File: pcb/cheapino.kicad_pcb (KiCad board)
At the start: 2 copper layers, 152.2 x 95.1 mm, 65 parts, among them K1 SW_Push, K10 SW_Push, K11 SW_Push, K12 SW_Push, K13 SW_Push, K14 SW_Push, K15 SW_Push, K16 SW_Push, K17 SW_Push, K18 SW_Push, K19 K19, K2 SW_Push, K20 K20, K21 K21, K3 SW_Push, K4 SW_Push, K5 SW_Push, K6 SW_Push, K7 SW_Push, K8 SW_Push, K9 SW_Push, U1 RP2040-Zero

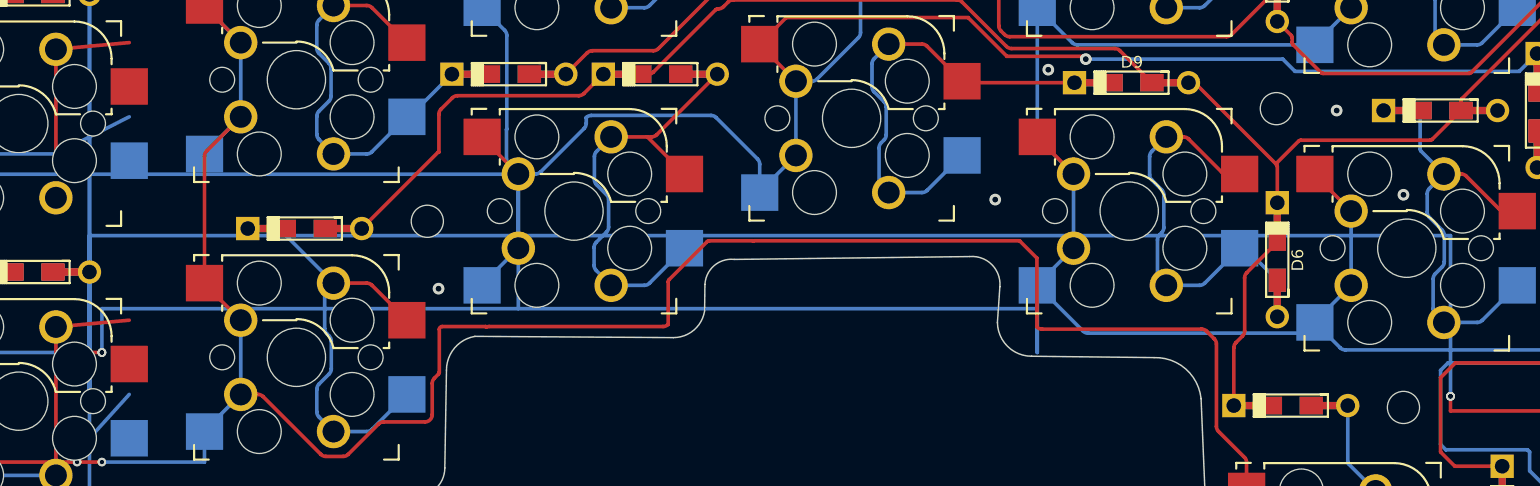
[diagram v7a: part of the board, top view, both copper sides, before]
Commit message: Re-route ROW_4 and COL_1 at y=90-92 through solid board, avoid cutout and holes
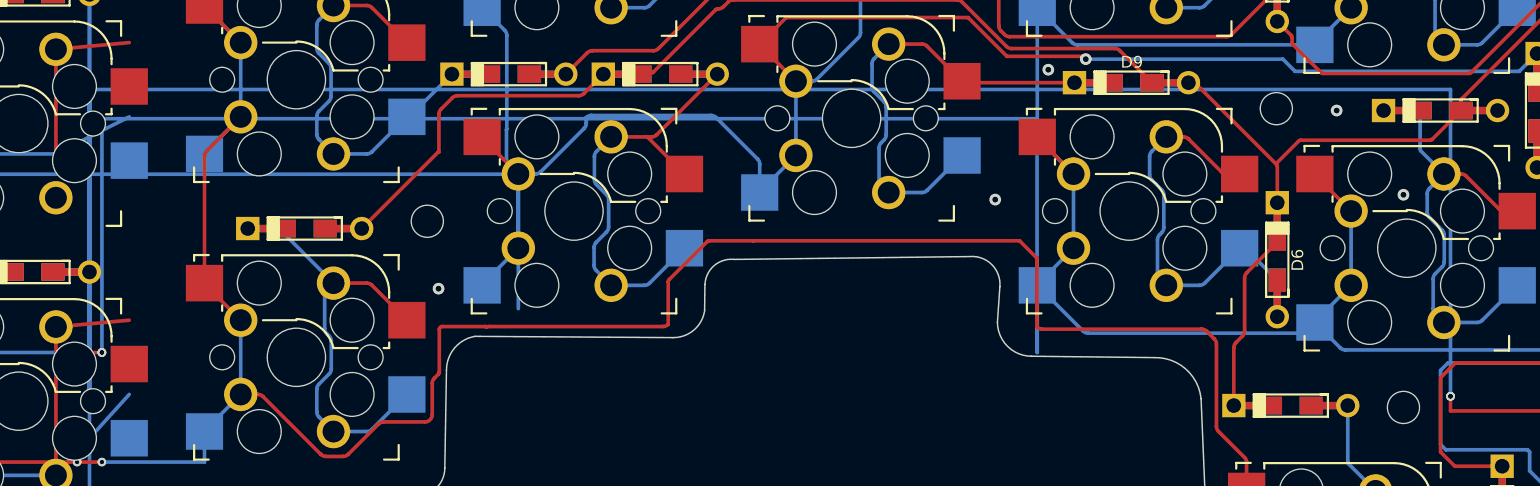
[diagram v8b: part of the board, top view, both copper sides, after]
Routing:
- net COL_1: track 385.9 -> 411.9 mm
- net ROW_4: track 270.5 -> 290.5 mm
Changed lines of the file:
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@@
 		)
 	)
+		(segment
+		(start 54.85 111.0)
+		(end 54.85 90.0)
+		(width 0.25)
+		(layer "B.Cu")
+		(net "ROW_4")
+	)
+	(segment
+		(start 54.85 90.0)
+		(end 148.0 90.0)
+		(width 0.25)
+		(layer "B.Cu")
+		(net "ROW_4")
+	)
+	(segment
+		(start 148.0 90.0)
+		(end 148.0 111.0)
+		(width 0.25)
+		(layer "B.Cu")
+		(net "ROW_4")
+	)
+	(via
+		(at 148.0 111.0)
+		(size 0.6)
+		(drill 0.3)
+		(layers "F.Cu" "B.Cu")
+		(net "ROW_4")
+	)
+	(via
+		(at 55.7 108.0)
+		(size 0.6)
+		(drill 0.3)
+		(layers "F.Cu" "B.Cu")
+		(net "COL_1")
+	)
+	(segment
+		(start 55.7 108.0)
+		(end 55.7 92.0)
+		(width 0.25)
+		(layer "B.Cu")
+		(net "COL_1")
+	)
+	(segment
+		(start 55.7 92.0)
+		(end 119.7 92.0)
+		(width 0.25)
+		(layer "B.Cu")
+		(net "COL_1")
+	)
 	(segment
+		(start 119.7 92.0)
+		(end 119.7 108.0)
+		(width 0.25)
+		(layer "B.Cu")
+		(net "COL_1")
+	)
+(segment
 		(start 163.131684 104.821883)
 		(end 163.708954 104.244613)
@@
 		(net "ROW_4")
 	)
-		(segment
-		(start 54.85 111.0)
-		(end 54.85 100.0)
-		(width 0.25)
-		(layer "B.Cu")
-		(net "ROW_4")
-	)
-	(segment
-		(start 54.85 100.0)
-		(end 148.0 100.0)
-		(width 0.25)
-		(layer "B.Cu")
-		(net "ROW_4")
-	)
-	(segment
-		(start 148.0 100.0)
-		(end 148.0 111.0)
-		(width 0.25)
-		(layer "B.Cu")
-		(net "ROW_4")
-	)
-	(via
-		(at 148.0 111.0)
-		(size 0.6)
-		(drill 0.3)
-		(layers "F.Cu" "B.Cu")
-		(net "ROW_4")
-	)
-	(via
-		(at 55.7 108.0)
-		(size 0.6)
-		(drill 0.3)
-		(layers "F.Cu" "B.Cu")
-		(net "COL_1")
-	)
-	(segment
-		(start 55.7 108.0)
-		(end 55.7 105.0)
-		(width 0.25)
-		(layer "B.Cu")
-		(net "COL_1")
-	)
-	(segment
-		(start 55.7 105.0)
-		(end 119.7 105.0)
-		(width 0.25)
-		(layer "B.Cu")
-		(net "COL_1")
-	)
-	(segment
-		(start 119.7 105.0)
-		(end 119.7 108.0)
-		(width 0.25)
-		(layer "B.Cu")
-		(net "COL_1")
-	)
 	(segment
